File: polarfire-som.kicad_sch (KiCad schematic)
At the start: 6 parts

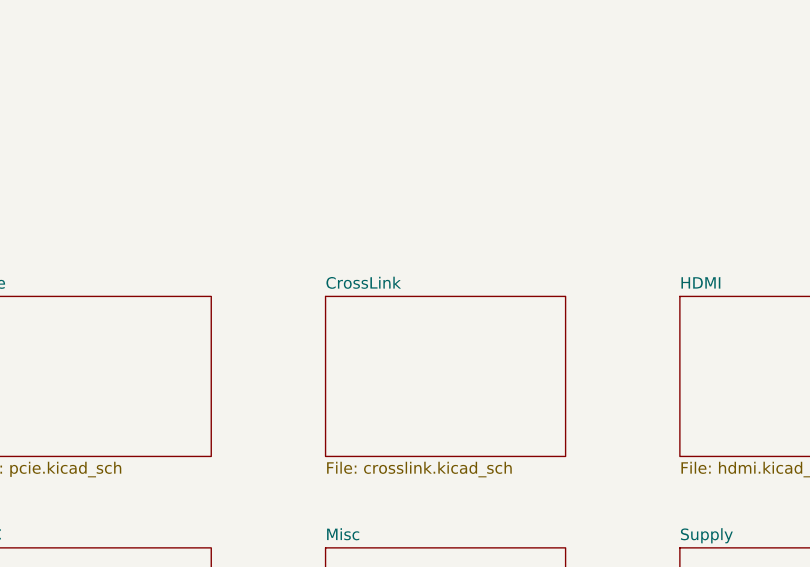
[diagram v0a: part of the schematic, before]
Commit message: [#53847] Connect PF SoC to CrossLink
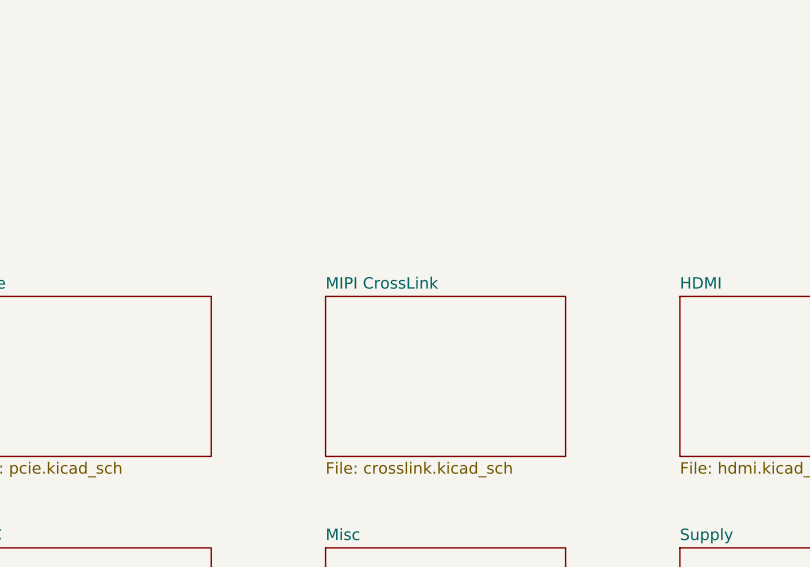
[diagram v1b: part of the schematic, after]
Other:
- sheet CrossLink renamed MIPI CrossLink
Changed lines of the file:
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@@
     (stroke (width 0.1524) (type solid) (color 0 0 0 0))
     (fill (color 0 0 0 0.0000))
-    (property "Sheet name" "CrossLink" (id 0) (at 130.81 107.2384 0)
+    (property "Sheet name" "MIPI CrossLink" (id 0) (at 130.81 107.2384 0)
       (effects (font (size 1.27 1.27)) (justify left bottom))
     )
@@
       (reference "N2") (unit 1) (value "oshw_logo") (footprint "antmicro-footprints:oshw-logo")
     )
-    (path "/99f116ae-bc8e-42a5-8f88-aecc401b3bcc/48b961bb-e84f-4162-9b4f-ee3835cef348"
-      (reference "U1") (unit 1) (value "MPFS250T-FCVG484") (footprint "antmicro-footprints:BGA-484_19x19mm_Layout22x22_P0.8mm_FCVG484")
-    )
     (path "/99f116ae-bc8e-42a5-8f88-aecc401b3bcc/33525ff0-ccdb-444b-b19d-33f381d75f01"
       (reference "U1") (unit 2) (value "MPFS250T-FCVG484") (footprint "antmicro-footprints:BGA-484_19x19mm_Layout22x22_P0.8mm_FCVG484")
@@
       (reference "U9") (unit 1) (value "CrossLink_LIF-MD6000-6JMG80I") (footprint "antmicro-footprints:BGA-80_7x7mm_Layout10x10_P0.65mm")
     )
+    (path "/99f116ae-bc8e-42a5-8f88-aecc401b3bcc/609f0bcc-8214-47d3-995a-9ea2c0b2ec63"
+      (reference "U?") (unit 1) (value "MPFS250T-FCVG484") (footprint "antmicro-footprints:BGA-484_19x19mm_Layout22x22_P0.8mm_FCVG484")
+    )
     (path "/9d03ca8b-00f4-4bc6-89d1-f3be2c1a83b3/6b7beb5c-67ba-4dca-8603-d8ff078ad5d4"

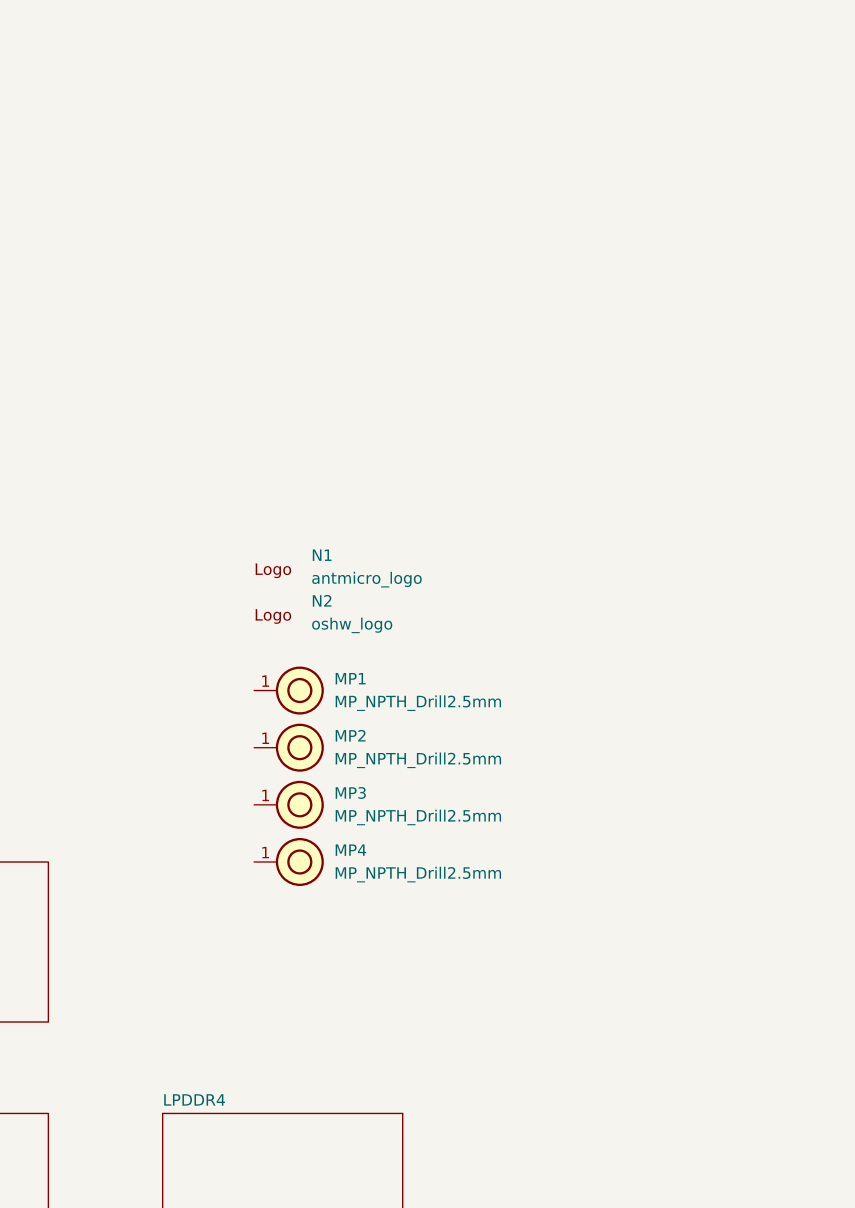
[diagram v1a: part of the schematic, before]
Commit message: [#53847] Add PCLK to Crosslink data transmission
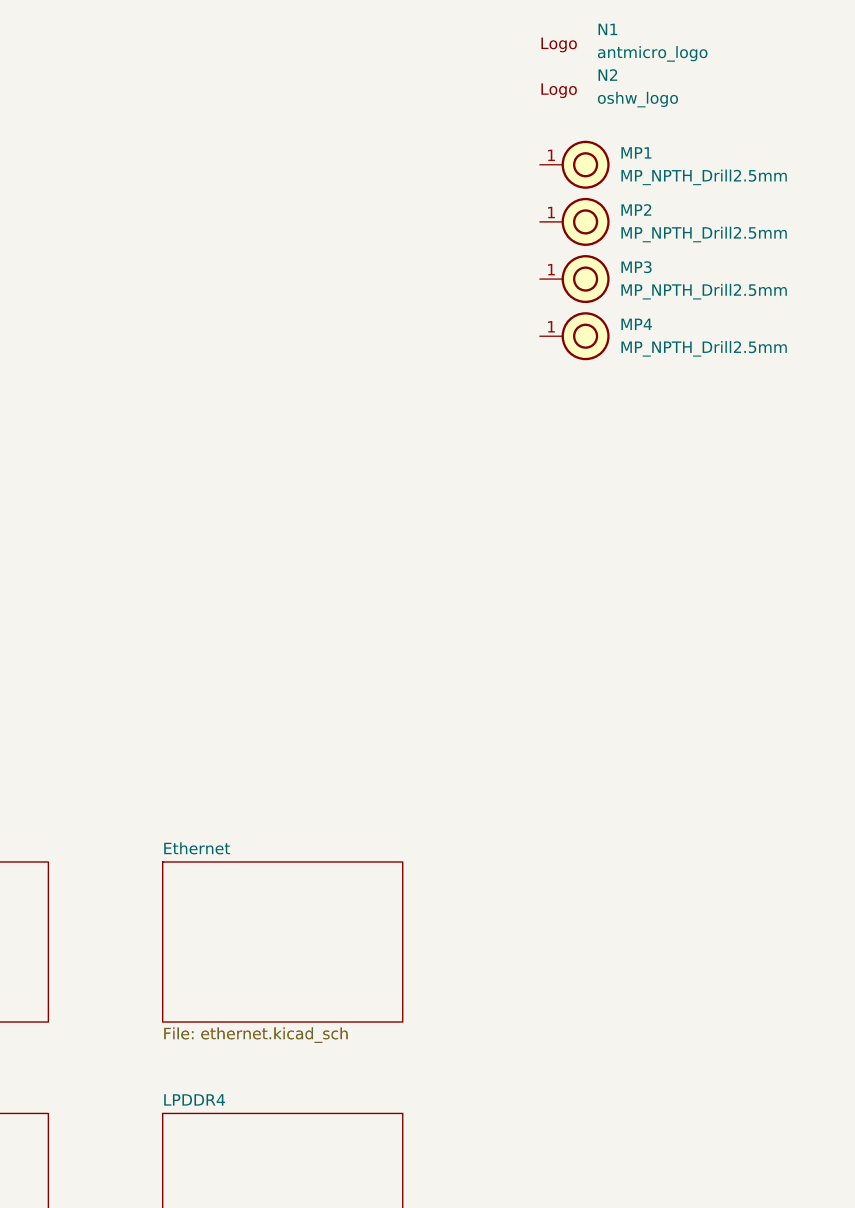
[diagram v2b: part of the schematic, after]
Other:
- added sheet Ethernet (ethernet.kicad_sch)
- moved on the sheet: MP1, MP2, MP3, MP4, N1, N2

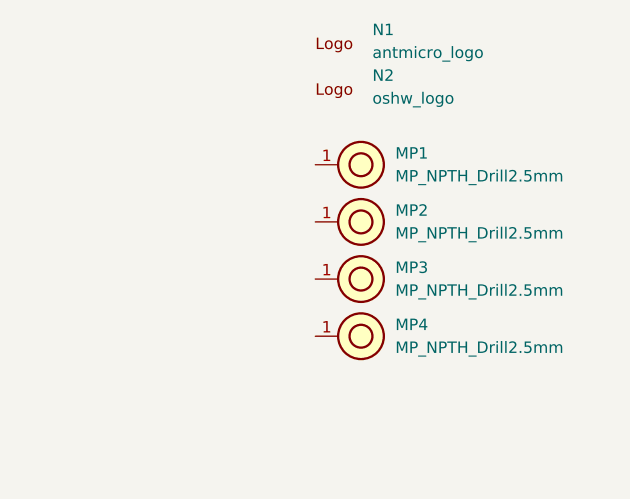
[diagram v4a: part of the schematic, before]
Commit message: [#52577] Clear annotations
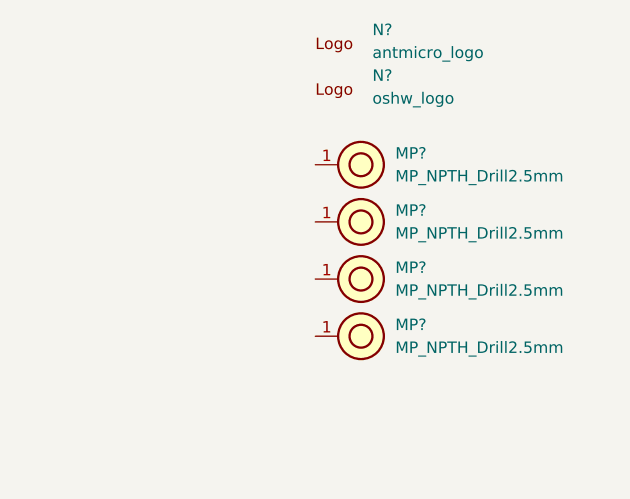
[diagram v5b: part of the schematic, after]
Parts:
- renumbered MP1 to MP?, MP4 to MP?, MP2 to MP?, MP3 to MP?, N2 to N?, N1 to N?

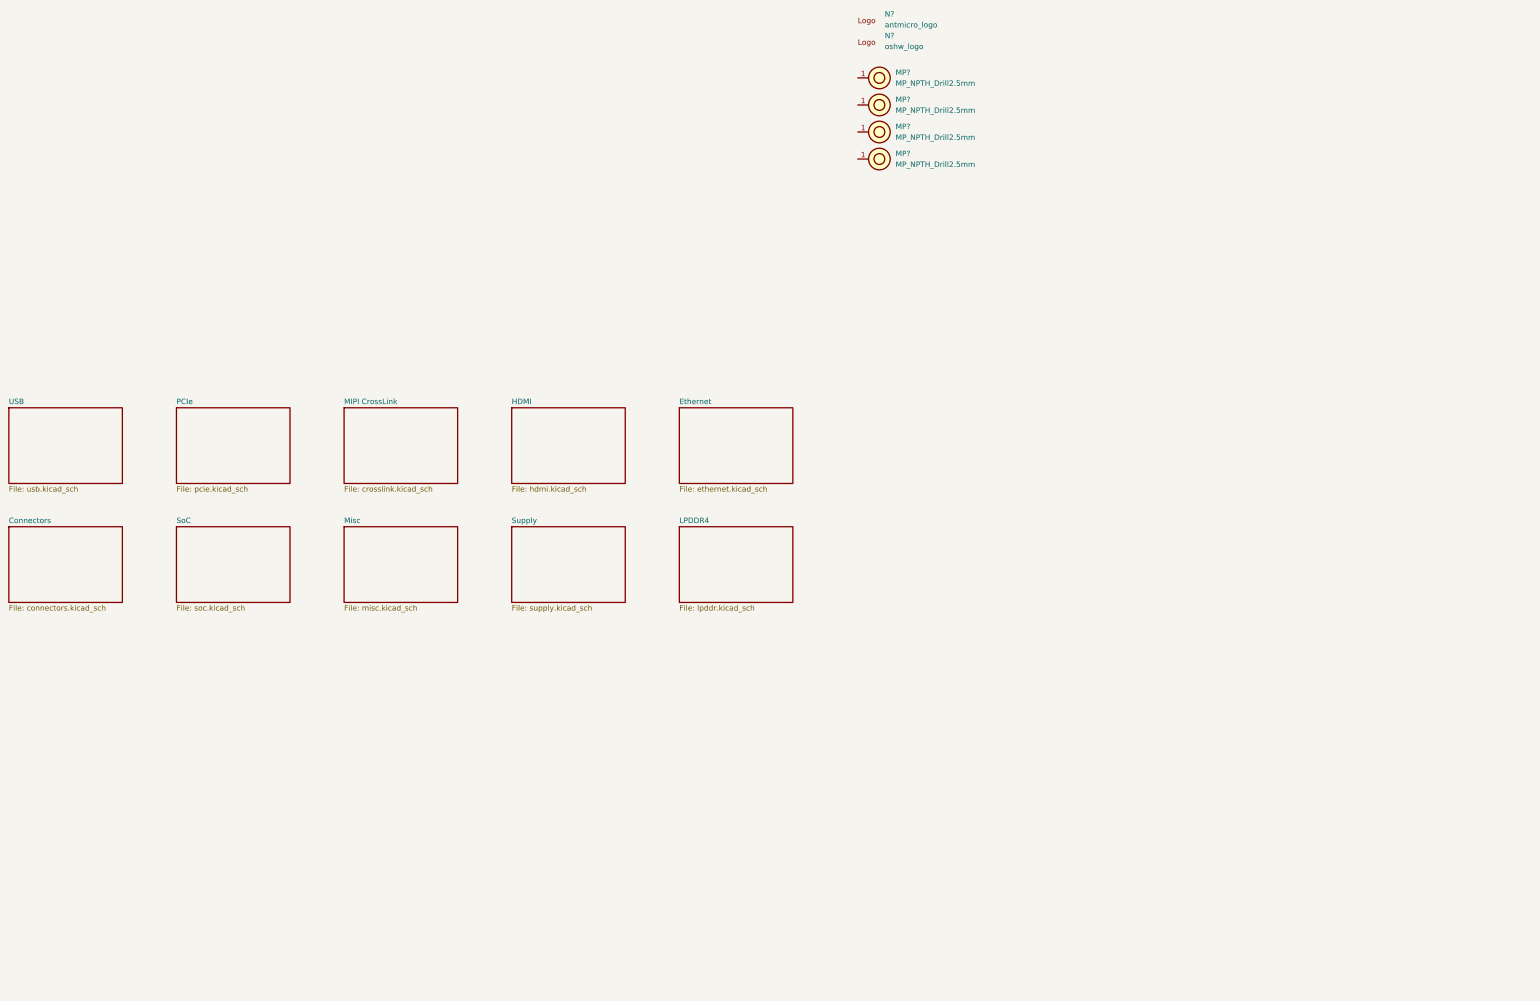
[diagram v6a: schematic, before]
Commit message: [#54084] Sheets cleanup
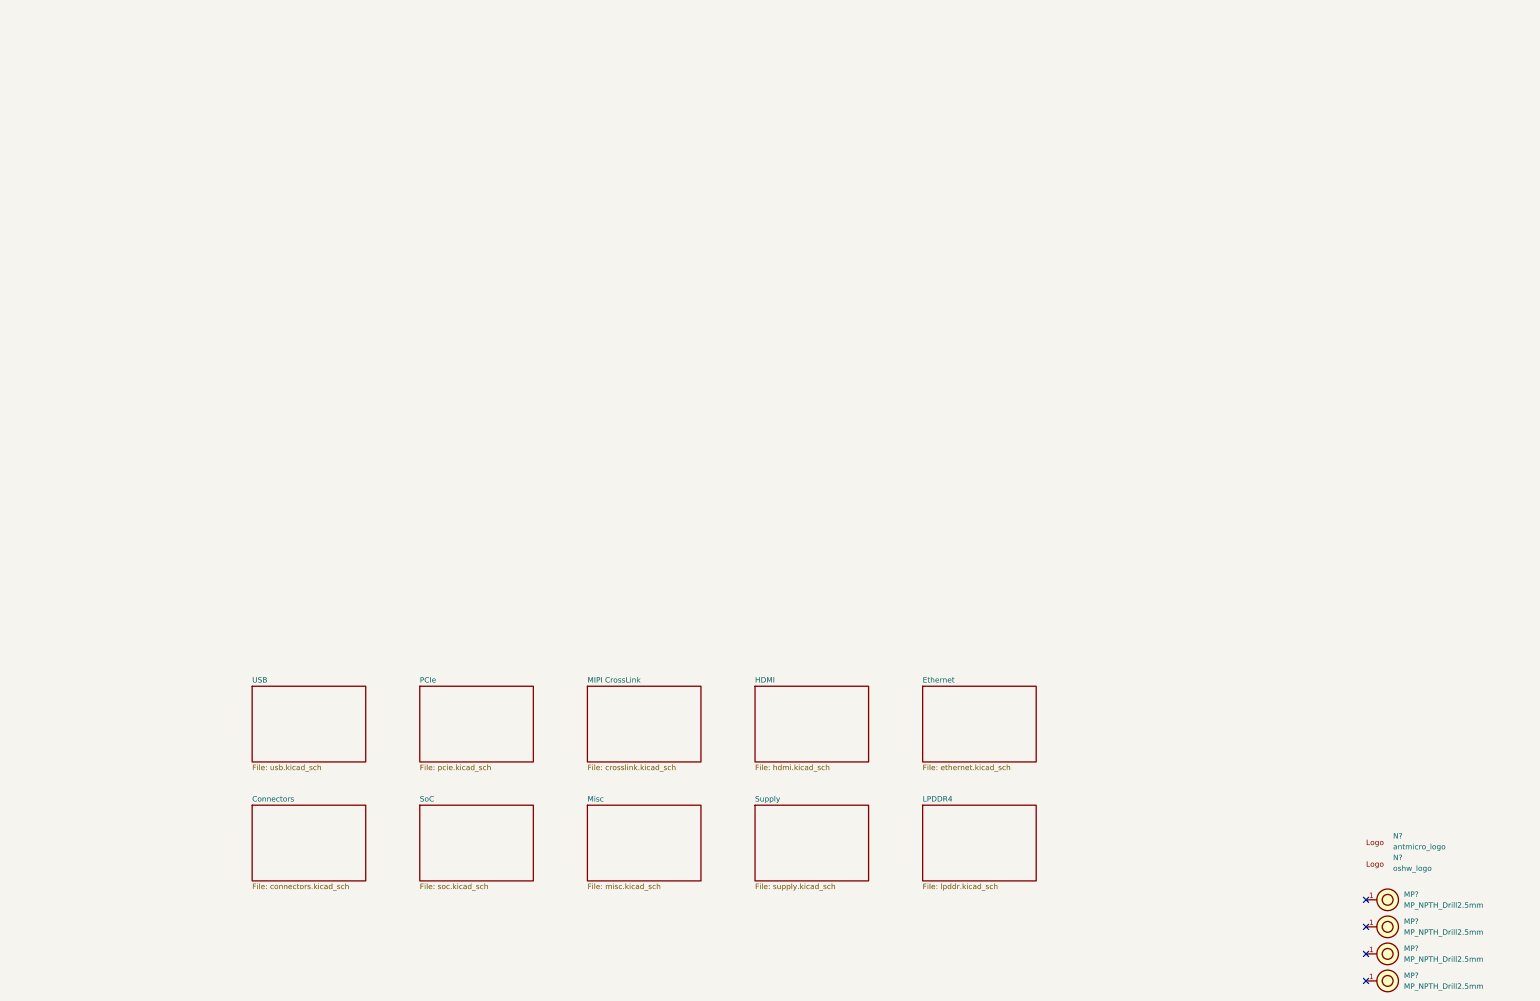
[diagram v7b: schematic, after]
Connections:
- no-connect marks 0 -> 4
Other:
- moved on the sheet: MP?, N?

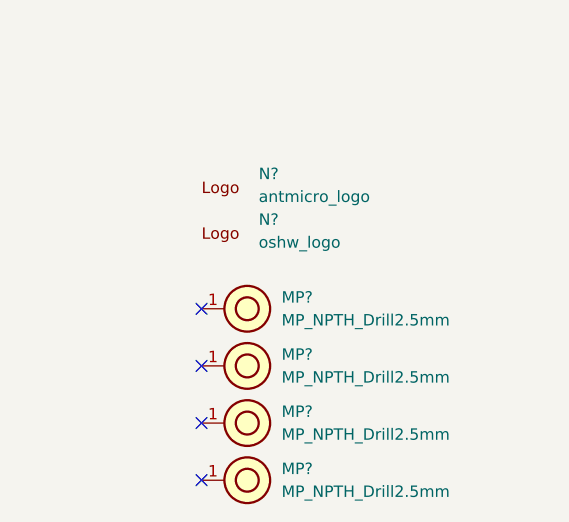
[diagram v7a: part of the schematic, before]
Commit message: [#54016] Place components to assess available space
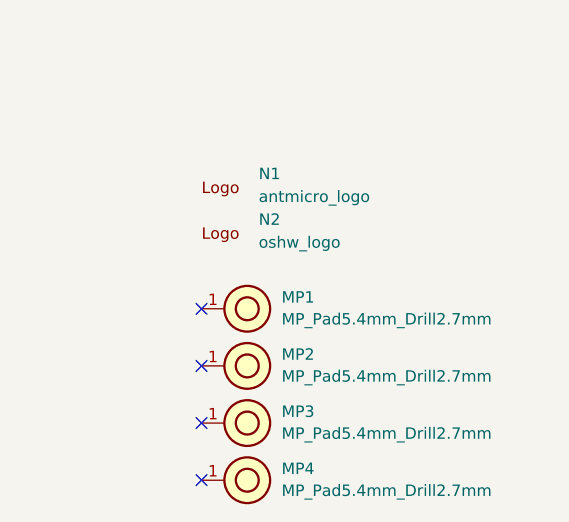
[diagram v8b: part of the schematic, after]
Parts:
- MP1, MP2, MP3, MP4: renamed from MP?; value MP_NPTH_Drill2.5mm -> MP_Pad5.4mm_Drill2.7mm; footprint antmicro-footprints:MP_NPTH_Drill2.5mm -> antmicro-footprints:MP_Pad5.4mm_Drill2.7mm; symbol antmicroMechanicalParts:MP_NPTH_Drill2.5mm -> antmicroMechanicalParts:MP_Pad5.4mm_Drill2.7mm
- N1: renamed from N?; footprint antmicro-footprints:antmicro-logo_scaled_12mm -> antmicro-footprints:antmicro-logo
- gave numbers to parts that had none: 1
